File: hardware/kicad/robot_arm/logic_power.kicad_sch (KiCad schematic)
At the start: 0 parts

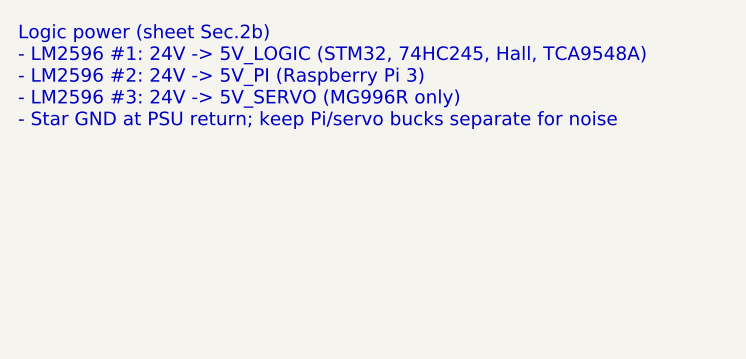
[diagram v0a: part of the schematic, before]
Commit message: docs: Update documentation and schematics to reflect transition from Raspberry Pi 3 to Raspberry Pi 4 for high-level control and power management. Adjusted references in README, calculations, design choices, examples, scope, and electrical schematics. Enhanced BOM and electrical interface documentation for improved clarity on power requirements and connections.
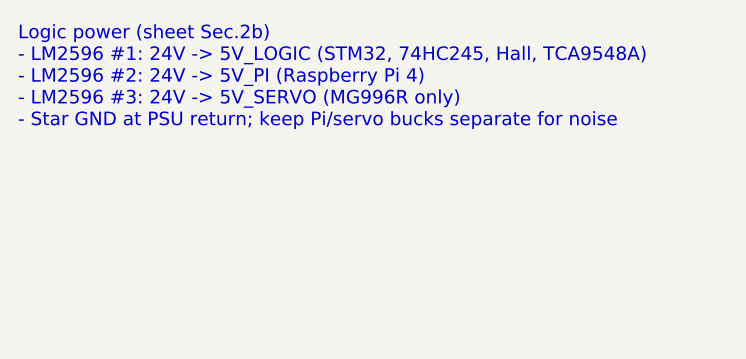
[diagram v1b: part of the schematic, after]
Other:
- note added: "Logic power (sheet Sec.2b) - LM2596 #1: 24V -> 5V_LOGIC (STM32, 74HC245, Hall, TCA9548A) - LM2596 #2: 24V -> 5V_PI (Raspberry Pi 4) - LM2596 #3: 24V -> 5V_SERVO (MG996R only) - Star GND at PSU return; keep Pi/servo bucks separate for noise"
- note removed: "Logic power (sheet Sec.2b) - LM2596 #1: 24V -> 5V_LOGIC (STM32, 74HC245, Hall, TCA9548A) - LM2596 #2: 24V -> 5V_PI (Raspberry Pi 3) - LM2596 #3: 24V -> 5V_SERVO (MG996R only) - Star GND at PSU return; keep Pi/servo bucks separate for noise"
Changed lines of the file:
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@@
 		(rev "0.1")
 	)
-	(text "Logic power (sheet Sec.2b)\n- LM2596 #1: 24V -> 5V_LOGIC (STM32, 74HC245, Hall, TCA9548A)\n- LM2596 #2: 24V -> 5V_PI (Raspberry Pi 3)\n- LM2596 #3: 24V -> 5V_SERVO (MG996R only)\n- Star GND at PSU return; keep Pi/servo bucks separate for noise"
+	(text "Logic power (sheet Sec.2b)\n- LM2596 #1: 24V -> 5V_LOGIC (STM32, 74HC245, Hall, TCA9548A)\n- LM2596 #2: 24V -> 5V_PI (Raspberry Pi 4)\n- LM2596 #3: 24V -> 5V_SERVO (MG996R only)\n- Star GND at PSU return; keep Pi/servo bucks separate for noise"
 		(exclude_from_sim no)
 		(at 15 15 0)
